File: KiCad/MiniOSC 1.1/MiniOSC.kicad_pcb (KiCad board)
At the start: 2 copper layers, 94.1 x 128.5 mm, 64 parts, among them J1 Conn_01x16_Female, J2 Conn_01x16_Male, J3 V_OCT_IN, J4 FM_IN, J5 PULSE_OUT, J6 SAW_OUT, J7 JST_BUS, J8 IDC_BUS, Q1 BC558, Q2 BC548, U1 TL074, U2 40106

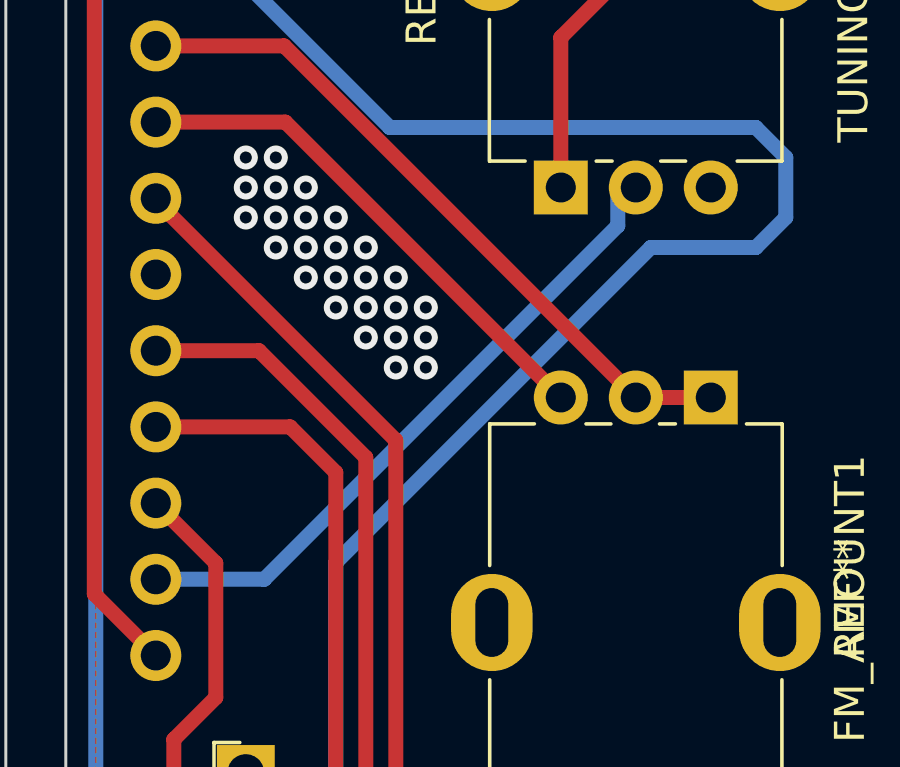
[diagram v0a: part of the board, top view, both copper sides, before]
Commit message: fixing traces on fine tuning 1.1 and 1.1 handscore
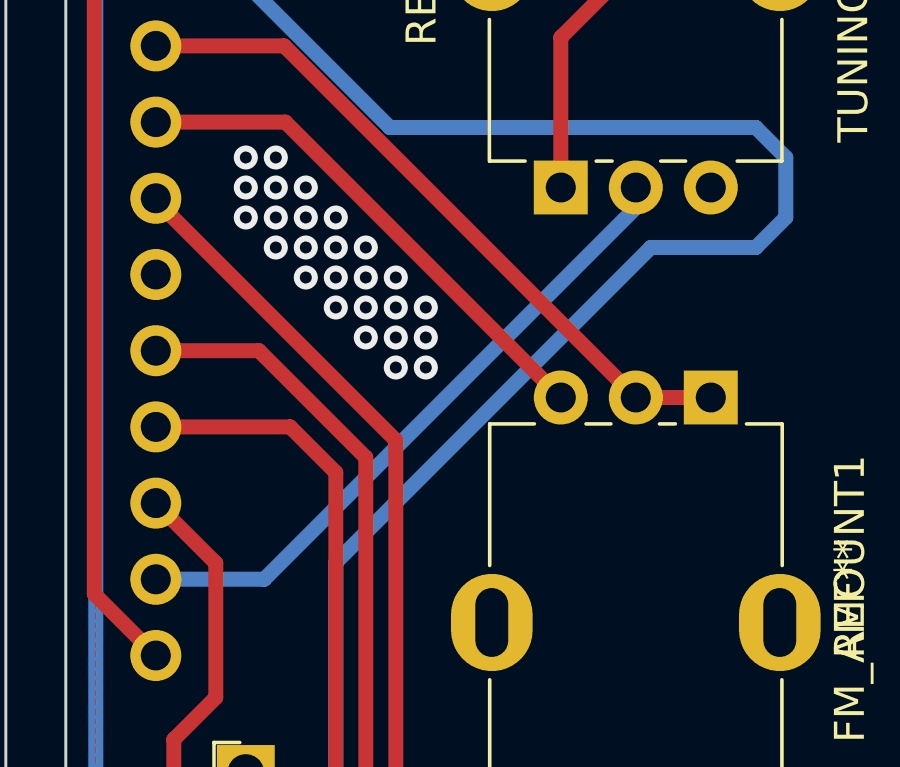
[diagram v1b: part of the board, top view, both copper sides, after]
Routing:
- net FP_12V_NEG: track 39.9 -> 39.4 mm
